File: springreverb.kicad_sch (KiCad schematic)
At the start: 61 parts, among them J1 IN, J10 To2, J11 To_Tank, J12 From_Tank, J13 FromGND, J14 From, J15 VR2_3, J16 VR2_3GND, J17 OUT, J2 INGND, J3 GND, J4 Vin, J5 VR1_2, J6 VR1_1, J8 ToGND, J9 To, U1 TL072, U2 TC1044S, U3 4556ADD

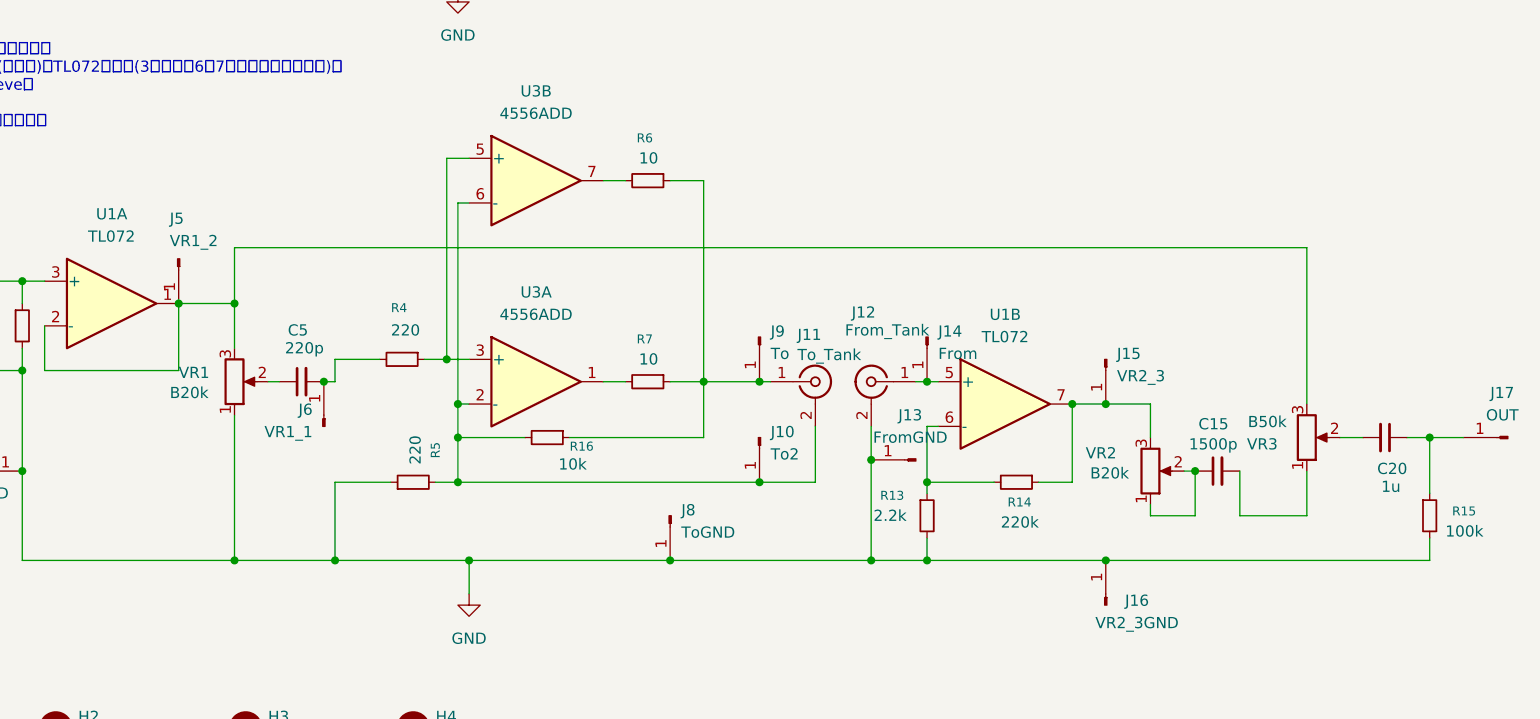
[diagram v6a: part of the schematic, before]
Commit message: 発振対策とVPの接続先を修正
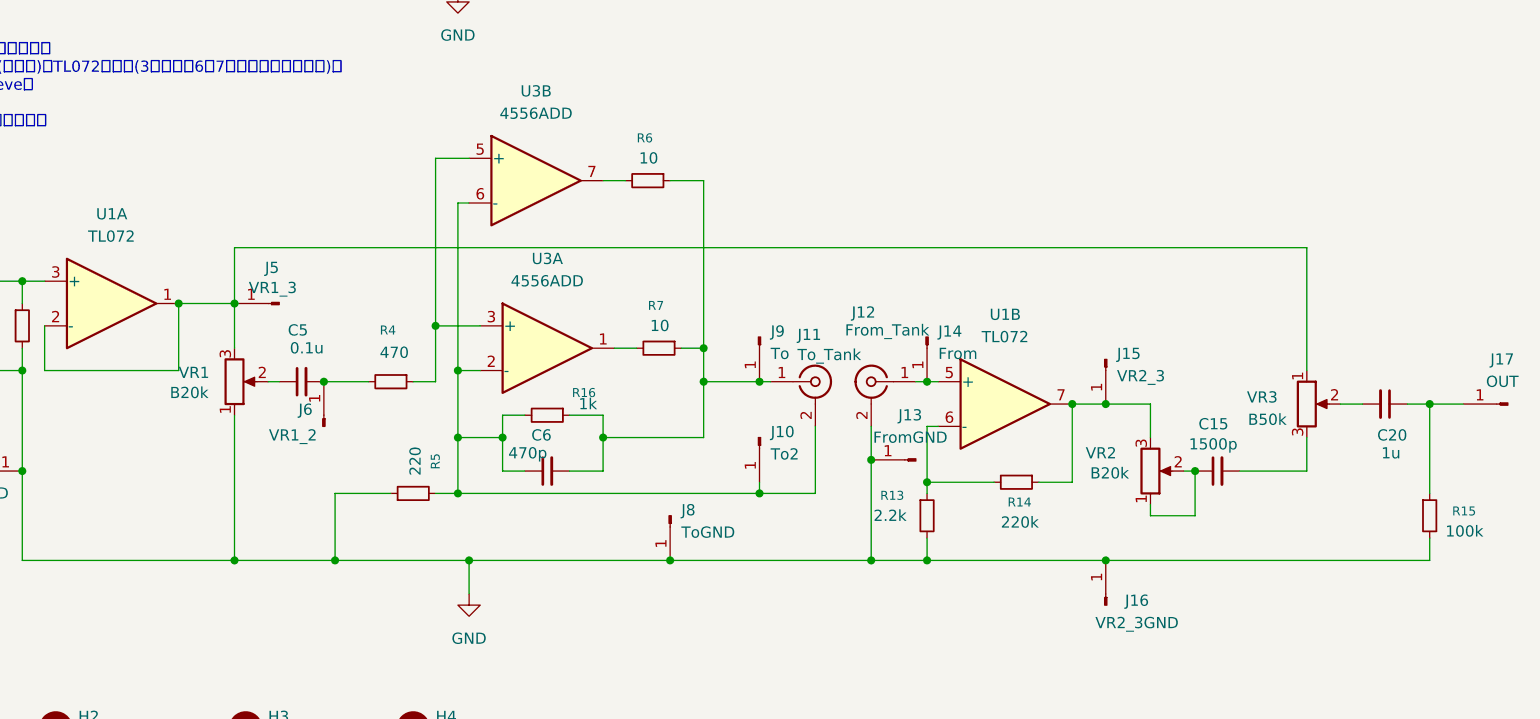
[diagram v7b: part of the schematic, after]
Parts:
- added C6: 470p, symbol Device:C_Small
- C5: value 220p -> 0.1u
- J5: value VR1_2 -> VR1_3
- J6: value VR1_1 -> VR1_2
- R16: value 10k -> 1k; footprint Resistor_THT:R_Axial_DIN0204_L3.6mm_D1.6mm_P7.62mm_Horizontal -> Resistor_THT:R_Axial_DIN0204_L3.6mm_D1.6mm_P2.54mm_Vertical
- R4: value 220 -> 470
- R5: footprint Resistor_THT:R_Axial_DIN0204_L3.6mm_D1.6mm_P7.62mm_Horizontal -> Resistor_THT:R_Axial_DIN0204_L3.6mm_D1.6mm_P2.54mm_Vertical
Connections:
- net at J10.1 (Pin_1), J11.2 (Ext), R16.2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: now also C6.1
- net at VR3.1: now also J5.1 (Pin_1), U1.1, U1.2 (-), VR1.3; no longer C15.2
- net at J11.1 (In), J9.1 (Pin_1), R16.1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: now also C6.2
- new net: C15.2, VR3.3
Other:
- moved on the sheet: C20, J17, J5, R16, R4, R5, R7, U3A, VR3

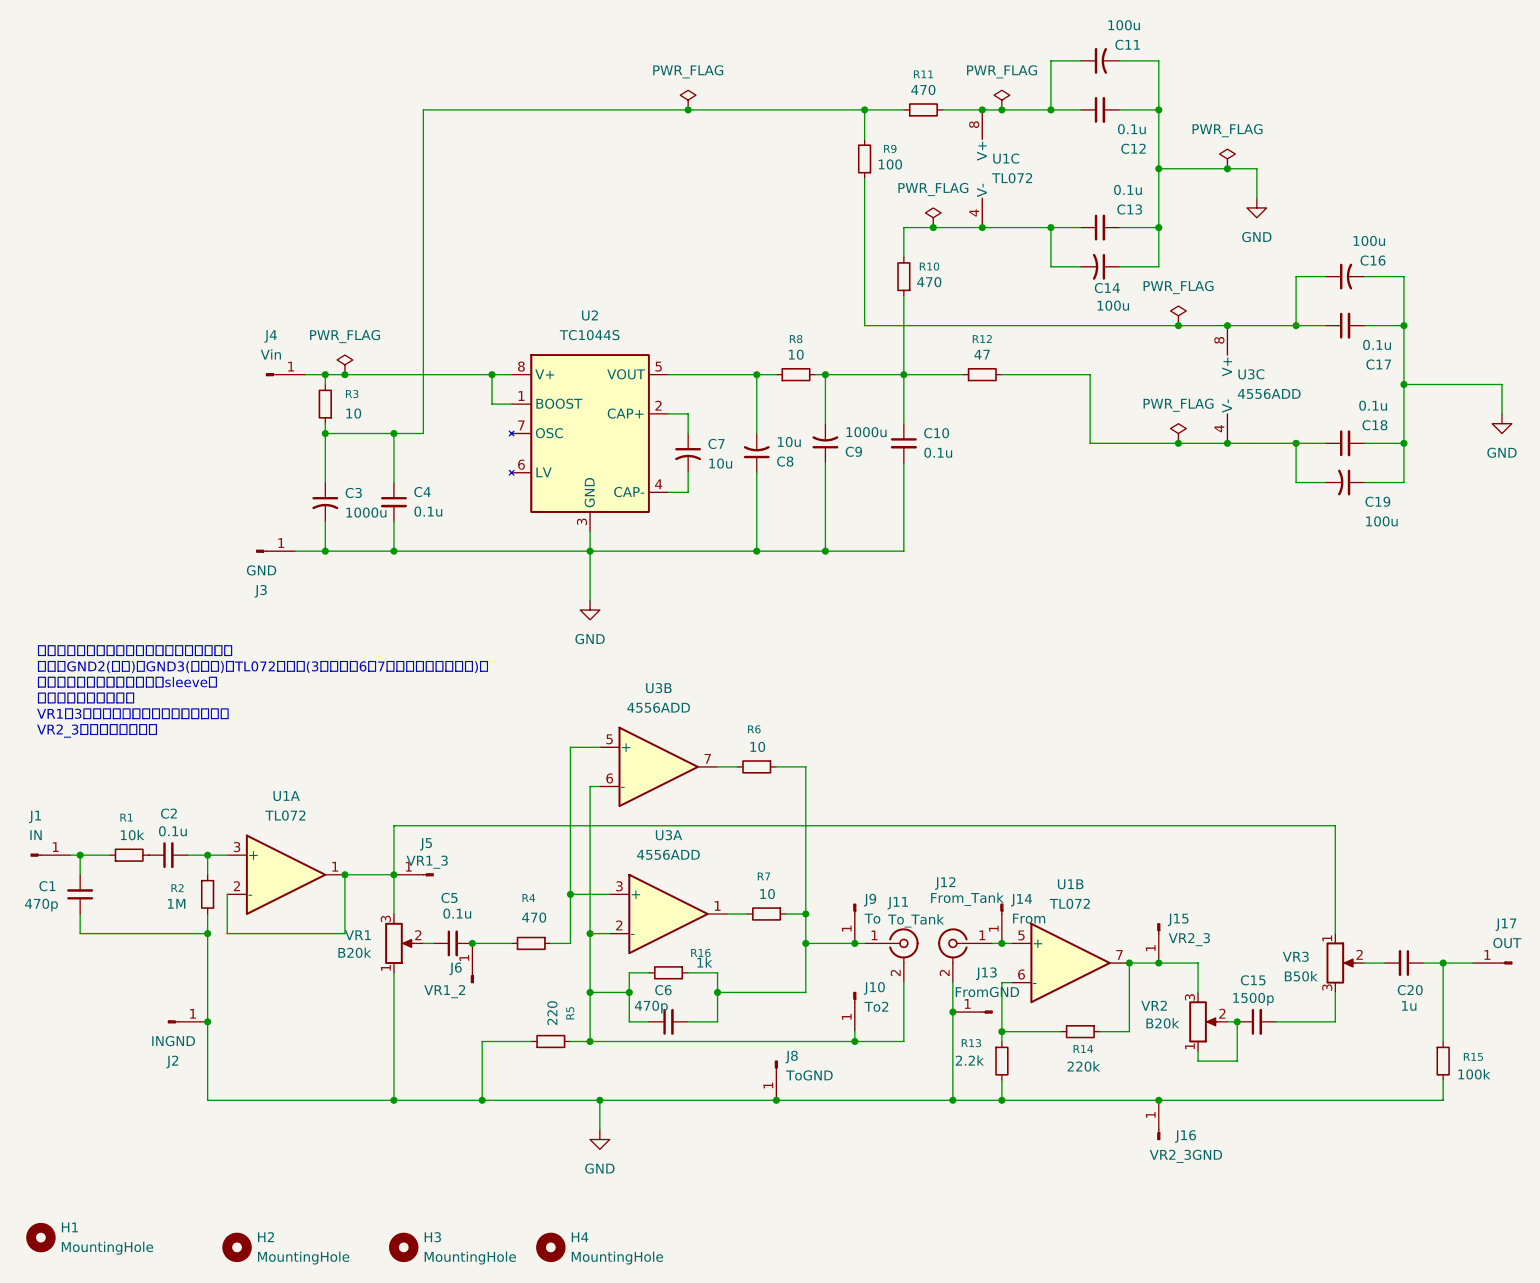
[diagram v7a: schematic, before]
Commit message: 増幅率やVR1とC5の前後を入れ替えたり
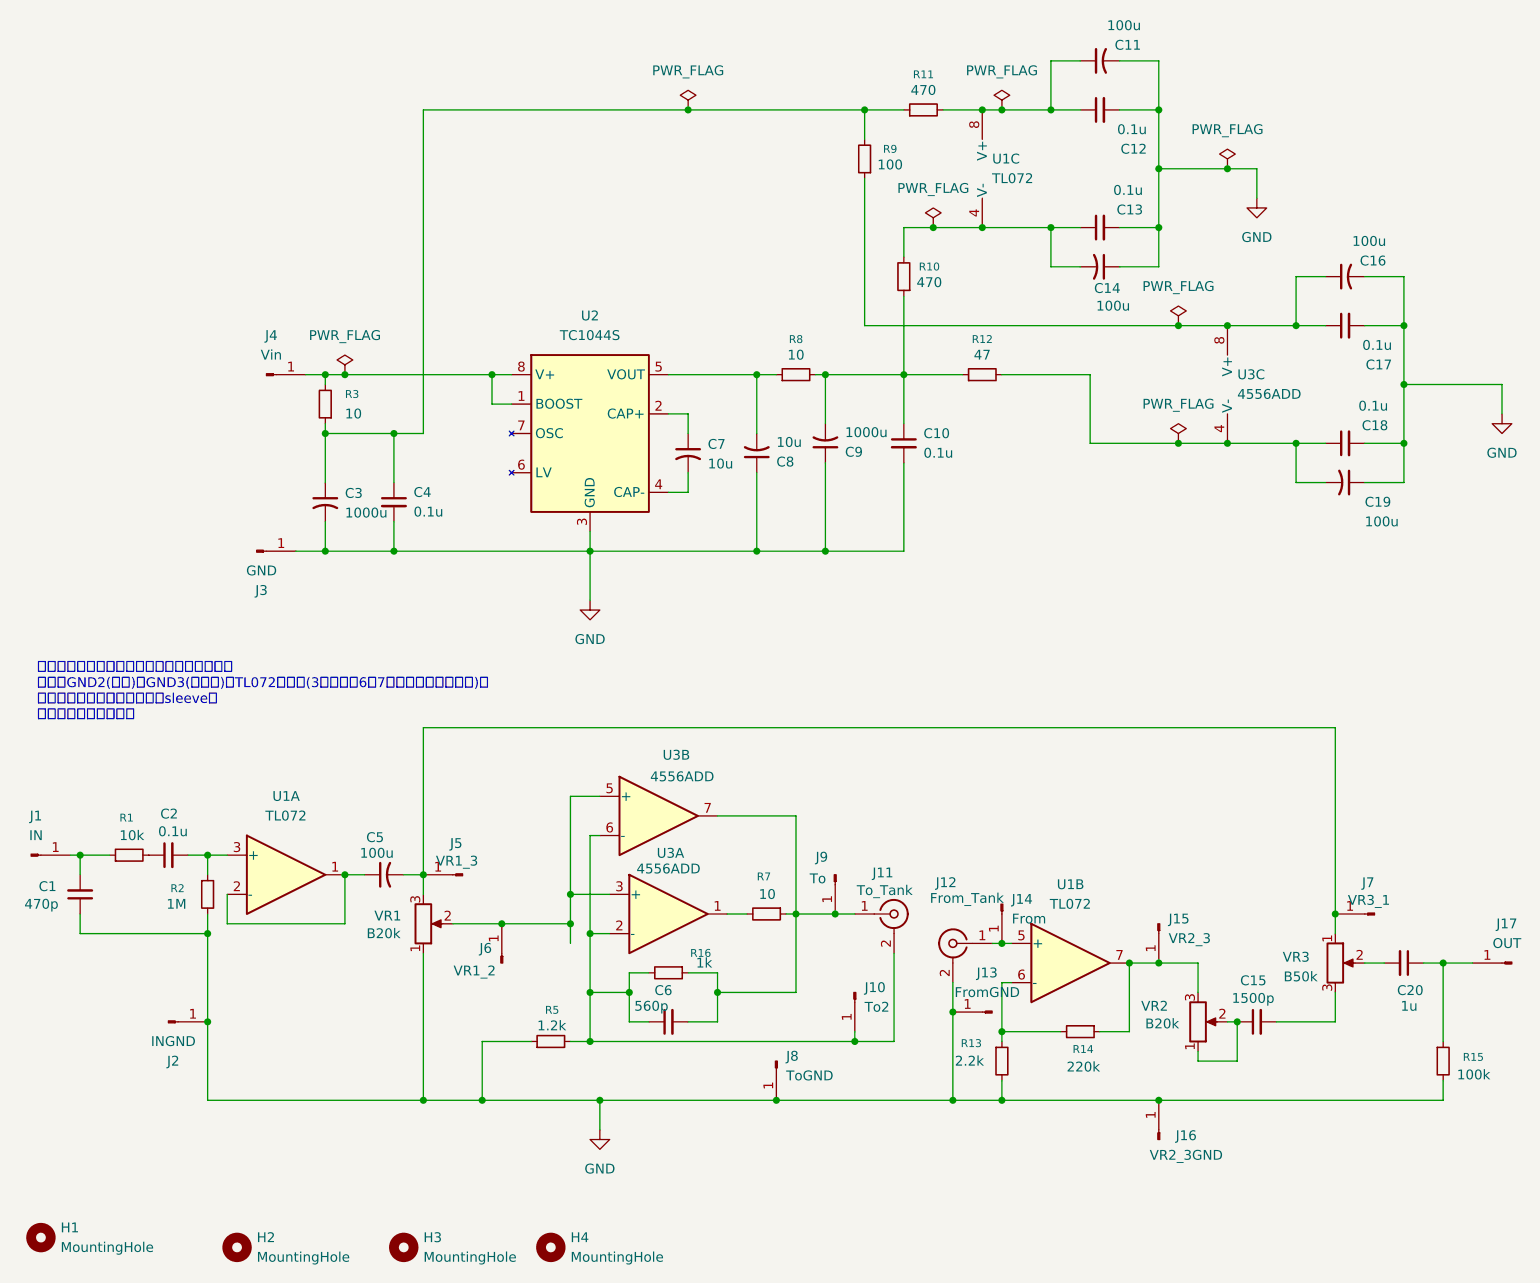
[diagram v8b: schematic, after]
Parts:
- removed C5: 0.1u, symbol Device:C_Small
- removed R4: 470, Resistor_THT:R_Axial_DIN0204_L3.6mm_D1.6mm_P7.62mm_Horizontal, symbol Device:R_Small
- removed R6: 10, Resistor_THT:R_Axial_DIN0204_L3.6mm_D1.6mm_P7.62mm_Horizontal, symbol Device:R_Small
- added C5: 100u, Capacitor_THT:CP_Radial_D6.3mm_P2.50mm, symbol Device:C_Small_US
- added J7: VR3_1, MyLibrary:PinHeader_1x01_P2.54mm_Vertical, symbol Connector:Conn_01x01_Pin
- C6: value 470p -> 560p
- R5: value 220 -> 1.2k
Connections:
- net at U3.3 (+), U3.5 (+): now also J6.1 (Pin_1), VR1.2
- net at U3.7: now also C6.2, J11.1 (In), J9.1 (Pin_1), R16.1, R7.1
- net at J5.1 (Pin_1), VR1.3, VR3.1: now also C5.2, J7.1 (Pin_1); no longer U1.1, U1.2 (-)
- new net: C5.1, U1.1, U1.2 (-)
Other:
- note added: "入力線はシールド線でだけど網線は片側接地 電源、GND2(回路)、GND3(タンク)はTL072の近く(3番ピンと6、7版番ピンの合流地点)で 合流させて一本でジャックのsleeveへ 入力は基板に片側接地"
- note removed: "入力線はシールド線でだけど網線は片側接地 電源、GND2(回路)、GND3(タンク)はTL072の近く(3番ピンと6、7版番ピンの合流地点)で 合流させて一本でジャックのsleeveへ 入力は基板に片側接地 VR1は3本シールド線でケースに片側接地 VR2_3は基板で片側接地"
- moved on the sheet: J11, J5, J6, J9, U3B, VR1
